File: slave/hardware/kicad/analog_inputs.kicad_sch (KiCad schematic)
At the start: 105 parts, among them IC10 TSV772IST, IC11 TSV772IST, IC12 TSV772IST, IC8 TSV772IST, IC9 TSV772IST

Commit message: feat(HW): start control sheet implementation
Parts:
- renumbered C38 to C20, C45 to C21, C44 to C22, C51 to C23, C40 to C24, C47 to C25, C39 to C26, C46 to C27, C52 to C28, C53 to C29, C54 to C30, C55 to C31, C41 to C32, C48 to C33, C42 to C34, C49 to C35, C56 to C36, C57 to C37, C43 to C38, C50 to C39, D24 to D10, D13 to D11, D20 to D12, D12 to D13, D19 to D14, D25 to D15, D26 to D16, D27 to D17, D28 to D18, D14 to D19, D21 to D20, D15 to D21, D29 to D23, D30 to D24, D16 to D25, D23 to D26, D11 to D7, D18 to D8, D17 to D9, IC8 to IC5, IC11 to IC6, IC9 to IC7, IC12 to IC8, IC10 to IC9, R20 to R10, R33 to R11, R22 to R12, R35 to R13, R24 to R14, R37 to R15, R30 to R16, R43 to R17, R44 to R18, R45 to R19, R46 to R20, R47 to R21, R48 to R22, R49 to R23, R19 to R24, R32 to R25, R21 to R26, R34 to R27, R23 to R28, R36 to R29, R25 to R30, R38 to R31, R50 to R32, R51 to R33, R52 to R34, R53 to R35, R54 to R36, R55 to R37, R56 to R38, R57 to R39, R26 to R40, R39 to R41, R27 to R42, R40 to R43, R28 to R44, R41 to R45, R29 to R46, R42 to R47, R18 to R8, R31 to R9, TP23 to TP10, TP10 to TP11, TP11 to TP12, TP14 to TP13, TP15 to TP14, TP24 to TP15, TP25 to TP16, TP26 to TP17, TP27 to TP18, TP16 to TP19, TP17 to TP20, TP18 to TP21, TP19 to TP22, TP28 to TP23, TP29 to TP24, TP20 to TP25, TP21 to TP26, TP13 to TP7, TP12 to TP8, TP22 to TP9

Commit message: feat(HW): add digital input circuit files
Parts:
- renumbered C20 to C40, C21 to C41, C22 to C42, C23 to C43, C24 to C44, C25 to C45, C26 to C46, C27 to C47, C28 to C48, C29 to C49, C30 to C50, C31 to C51, C32 to C52, C33 to C53, C34 to C54, C35 to C55, C36 to C56, C37 to C57, C38 to C58, C39 to C59, D7 to D27, D8 to D28, D9 to D29, D10 to D30, D11 to D31, D12 to D32, D13 to D33, D14 to D34, D15 to D35, D16 to D36, D17 to D37, D18 to D38, D19 to D39, D20 to D40, D21 to D41, D22 to D42, D23 to D43, D24 to D44, D25 to D45, D26 to D46, IC5 to IC10, IC6 to IC11, IC7 to IC12, IC8 to IC13, IC9 to IC14, R8 to R48, R9 to R49, R10 to R50, R11 to R51, R12 to R52, R13 to R53, R14 to R54, R15 to R55, R16 to R56, R17 to R57, R18 to R58, R19 to R59, R20 to R60, R21 to R61, R22 to R62, R23 to R63, R24 to R64, R25 to R65, R26 to R66, R27 to R67, R28 to R68, R29 to R69, R30 to R70, R31 to R71, R32 to R72, R33 to R73, R34 to R74, R35 to R75, R36 to R76, R37 to R77, R38 to R78, R39 to R79, R40 to R80, R41 to R81, R42 to R82, R43 to R83, R44 to R84, R45 to R85, R46 to R86, R47 to R87, TP7 to TP27, TP8 to TP28, TP9 to TP29, TP10 to TP30, TP11 to TP31, TP12 to TP32, TP13 to TP33, TP14 to TP34, TP15 to TP35, TP16 to TP36, TP17 to TP37, TP18 to TP38, TP19 to TP39, TP20 to TP40, TP21 to TP41, TP22 to TP42, TP23 to TP43, TP24 to TP44, TP25 to TP45, TP26 to TP46

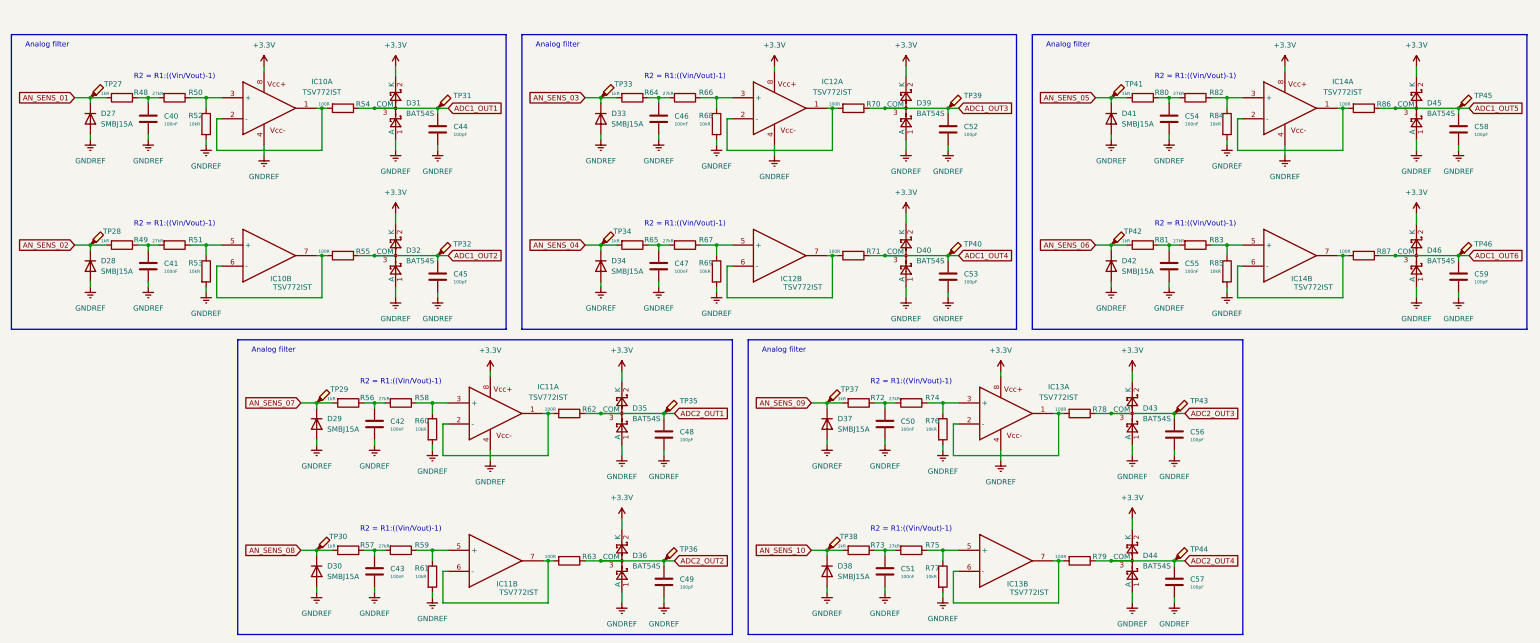
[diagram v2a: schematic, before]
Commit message: refactor(HW): reduce analog inputs and update MCU analog connections
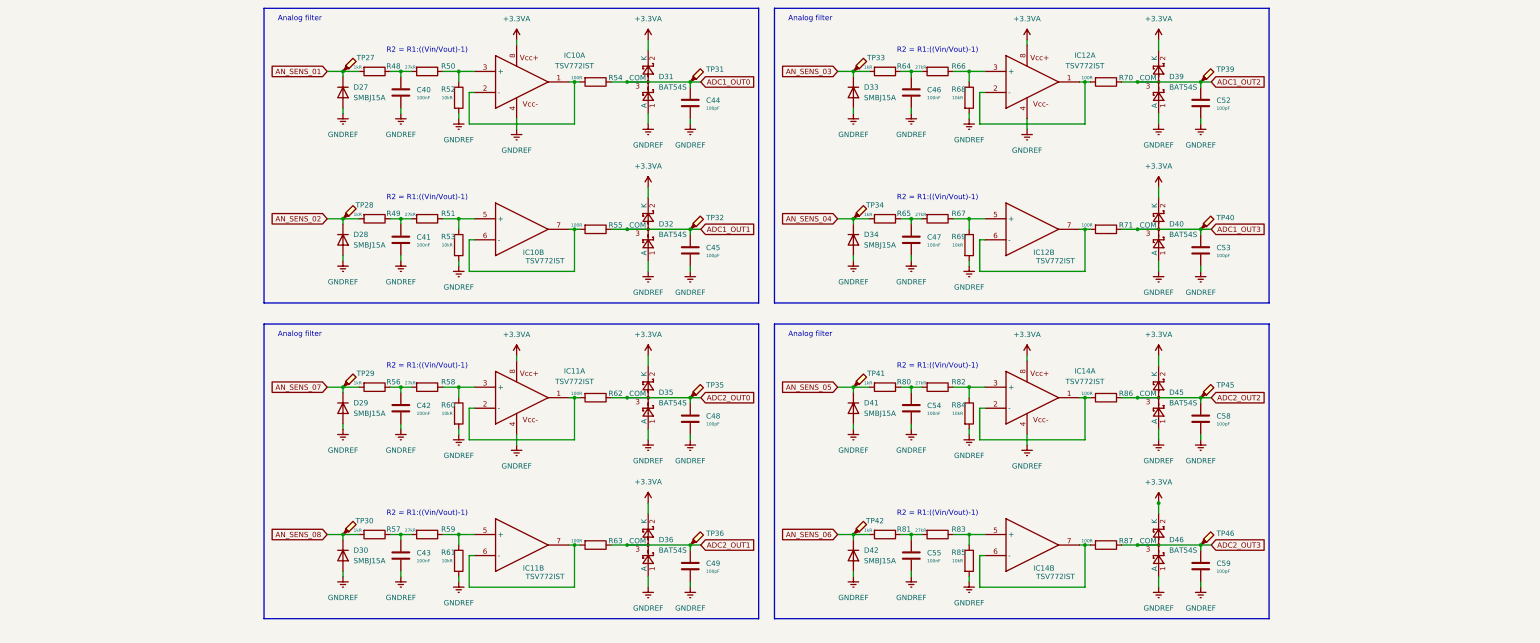
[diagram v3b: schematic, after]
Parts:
- removed C50, C51: 100nF, Capacitor_SMD:C_0201_0603Metric, symbol Device:C
- removed C56, C57: 100pF, Capacitor_SMD:C_0201_0603Metric, symbol Device:C
- removed D37, D38: SMBJ15A, Diode_SMD:D_SMB, symbol Device:D
- removed D43, D44: BAT54S, Package_TO_SOT_SMD:SOT-23, symbol Diode:BAT54S
- removed IC13: TSV772IST, SOP65P490X110-8N, symbol Datalogger Slave:TSV772IST
- removed R72, R73: 1kR, Resistor_SMD:R_0805_2012Metric, symbol Device:R
- removed R74, R75: 27kR, Resistor_SMD:R_0805_2012Metric, symbol Device:R
- removed R76, R77: 10kR, Resistor_SMD:R_0805_2012Metric, symbol Device:R
- removed R78, R79: 100R, Resistor_SMD:R_0805_2012Metric, symbol Device:R
- removed TP37, TP38, TP43, TP44: (no value), TestPoint:TestPoint_Pad_2.0x2.0mm, symbol Connector:TestPoint_Probe
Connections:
- net ADC1_OUT4 is gone; now on net ADC1_OUT3: C53.1, D40.3 (COM), R71.1, TP40.1
- net ADC1_OUT5 is gone; now on net ADC2_OUT2: C58.1, D45.3 (COM), R86.1, TP45.1
- net ADC1_OUT6 is gone; now on net ADC2_OUT3: C59.1, D46.3 (COM), R87.1, TP46.1
- net ADC1_OUT1: now also C45.1, D32.3 (COM), R55.1, TP32.1; no longer C44.1, D31.3 (COM), R54.1, TP31.1
- net ADC1_OUT2: now also C52.1, D39.3 (COM), R70.1, TP39.1; no longer C45.1, D32.3 (COM), R55.1, TP32.1
- net ADC1_OUT3: no longer C52.1, D39.3 (COM), R70.1, TP39.1
- net ADC2_OUT1: now also C49.1, D36.3 (COM), R63.1, TP36.1; no longer C48.1, D35.3 (COM), R62.1, TP35.1
- net ADC2_OUT2: no longer C49.1, D36.3 (COM), R63.1, TP36.1
- net +3.3V renamed +3.3VA
- new net ADC1_OUT0: C44.1, D31.3 (COM), R54.1, TP31.1
- new net ADC2_OUT0: C48.1, D35.3 (COM), R62.1, TP35.1
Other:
- moved on the sheet: C40, C41, C42, C43, C44, C45, C46, C47, C48, C49, C52, C53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

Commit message: feat(HW): create communication schematic with CAN and I2C level shifter
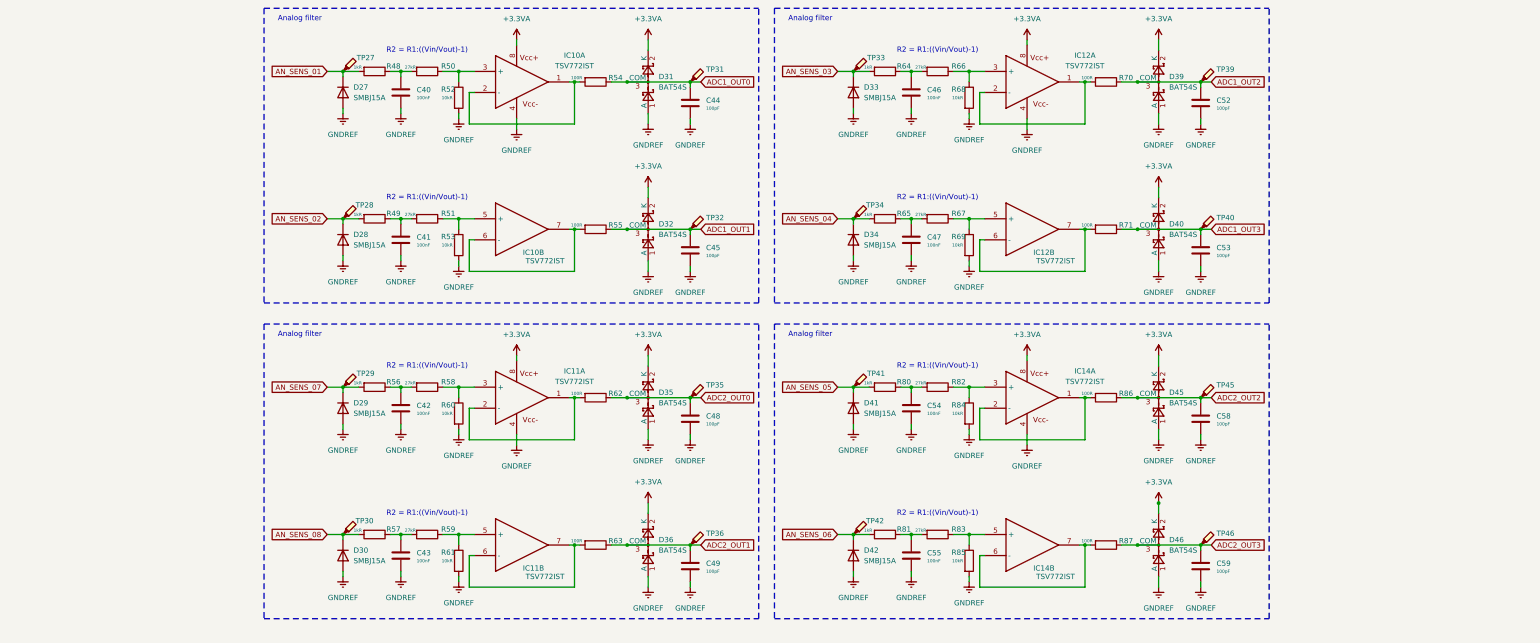
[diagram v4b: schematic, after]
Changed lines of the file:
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@@
 		(stroke
 			(width 0)
-			(type default)
+			(type dash_dot)
 		)
 	)
@@
 		(stroke
 			(width 0)
-			(type default)
+			(type dash_dot)
 		)
 	)
@@
 		(stroke
 			(width 0)
-			(type default)
+			(type dash_dot)
 		)
 	)
@@
 		(stroke
 			(width 0)
-			(type default)
+			(type dash_dot)
 		)
 	)
@@
 		(stroke
 			(width 0)
-			(type default)
+			(type dash_dot)
 		)
 	)
@@
 		(stroke
 			(width 0)
-			(type default)
+			(type dash_dot)
 		)
 	)
@@
 		(stroke
 			(width 0)
-			(type default)
+			(type dash_dot)
 		)
 	)
@@
 		(stroke
 			(width 0)
-			(type default)
+			(type dash_dot)
 		)
 	)
@@
 		(stroke
 			(width 0)
-			(type default)
+			(type dash_dot)
 		)
 	)
@@
 		(stroke
 			(width 0)
-			(type default)
+			(type dash_dot)
 		)
 	)
@@
 		(stroke
 			(width 0)
-			(type default)
+			(type dash_dot)
 		)
 	)
@@
 		(stroke
 			(width 0)
-			(type default)
+			(type dash_dot)
 		)
 	)
@@
 		(stroke
 			(width 0)
-			(type default)
+			(type dash_dot)
 		)
 	)
@@
 		(stroke
 			(width 0)
-			(type default)
+			(type dash_dot)
 		)
 	)
@@
 		(stroke
 			(width 0)
-			(type default)
+			(type dash_dot)
 		)
 	)
@@
 		(stroke
 			(width 0)
-			(type default)
-		)
-	)
+			(type dash_dot)
+		)
+	)

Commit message: refactor(HW): rename components and fix reference designators
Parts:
- renumbered C40 to C20, C41 to C21, C42 to C22, C43 to C23, C44 to C24, C45 to C25, C48 to C26, C49 to C27, C46 to C28, C47 to C29, C54 to C30, C55 to C31, C52 to C32, C53 to C33, C58 to C34, C59 to C35, D30 to D10, D31 to D11, D32 to D12, D35 to D13, D36 to D14, D33 to D15, D34 to D16, D41 to D17, D42 to D18, D39 to D19, D40 to D20, D45 to D21, D46 to D22, D27 to D7, D28 to D8, D29 to D9, IC10 to IC5, IC11 to IC6, IC12 to IC7, IC14 to IC8, R56 to R10, R57 to R11, R50 to R12, R51 to R13, R58 to R14, R59 to R15, R52 to R16, R53 to R17, R60 to R18, R61 to R19, R54 to R20, R55 to R21, R62 to R22, R63 to R23, R64 to R24, R65 to R25, R80 to R26, R81 to R27, R66 to R28, R67 to R29, R82 to R30, R83 to R31, R68 to R32, R69 to R33, R84 to R34, R85 to R35, R70 to R36, R71 to R37, R86 to R38, R87 to R39, R48 to R8, R49 to R9, TP30 to TP10, TP31 to TP11, TP32 to TP12, TP35 to TP13, TP36 to TP14, TP33 to TP15, TP34 to TP16, TP41 to TP17, TP42 to TP18, TP39 to TP19, TP40 to TP20, TP45 to TP21, TP46 to TP22, TP27 to TP7, TP28 to TP8, TP29 to TP9
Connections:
- net AN_SENS_05: now also D9.1 (K), R10.2, TP9.1; no longer D17.1 (K), R26.2, TP17.1
- net AN_SENS_06: now also D10.1 (K), R11.2, TP10.1; no longer D18.1 (K), R27.2, TP18.1
- net AN_SENS_07: now also D17.1 (K), R26.2, TP17.1; no longer D9.1 (K), R10.2, TP9.1
- net AN_SENS_08: now also D18.1 (K), R27.2, TP18.1; no longer D10.1 (K), R11.2, TP10.1

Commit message: feat(HW): add footprints and configure component properties
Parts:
- IC5, IC6, IC7, IC8: footprint SOP65P490X110-8N -> Datalogger:SOP65P490X110-8N
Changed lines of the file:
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@@
 			)
 		)
-		(property "Footprint" "SOP65P490X110-8N"
+		(property "Footprint" "Datalogger:SOP65P490X110-8N"
 			(at 284.48 190.17 0)
 			(hide yes)
@@
 			)
 		)
-		(property "Footprint" "SOP65P490X110-8N"
+		(property "Footprint" "Datalogger:SOP65P490X110-8N"
 			(at 161.29 225.73 0)
 			(hide yes)
@@
 			)
 		)
-		(property "Footprint" "SOP65P490X110-8N"
+		(property "Footprint" "Datalogger:SOP65P490X110-8N"
 			(at 161.29 266.37 0)
 			(hide yes)
@@
 			)
 		)
-		(property "Footprint" "SOP65P490X110-8N"
+		(property "Footprint" "Datalogger:SOP65P490X110-8N"
 			(at 284.48 225.73 0)
 			(hide yes)
@@
 			)
 		)
-		(property "Footprint" "SOP65P490X110-8N"
+		(property "Footprint" "Datalogger:SOP65P490X110-8N"
 			(at 161.29 301.93 0)
 			(hide yes)
@@
 			)
 		)
-		(property "Footprint" "SOP65P490X110-8N"
+		(property "Footprint" "Datalogger:SOP65P490X110-8N"
 			(at 284.48 266.37 0)
 			(hide yes)
@@
 			)
 		)
-		(property "Footprint" "SOP65P490X110-8N"
+		(property "Footprint" "Datalogger:SOP65P490X110-8N"
 			(at 284.48 301.93 0)
 			(hide yes)
@@
 			)
 		)
-		(property "Footprint" "SOP65P490X110-8N"
+		(property "Footprint" "Datalogger:SOP65P490X110-8N"
 			(at 161.29 190.17 0)
 			(hide yes)

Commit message: fix(HW): resolve KiCad ERC warnings
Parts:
- removed IC5, IC6, IC7, IC8: TSV772IST, Datalogger:SOP65P490X110-8N, symbol Datalogger Slave:TSV772IST
- added IC5, IC6, IC7, IC9: TSV772IST, Datalogger:SOP65P490X110-8N, symbol Datalogger:TSV772IST
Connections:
- net +3.3VA: now also IC5.8, IC6.8, IC7.8, IC9.8
- net GNDREF: now also IC5.4, IC6.4, IC7.4, IC9.4
- net at R23.2: now also IC7.6 (-), IC7.7
- net at R36.2: now also IC5.1, IC5.2 (-)
- net at R28.1, R32.1: now also IC5.3 (+)
- net at R30.1, R34.1: now also IC6.3 (+)
- net at R29.1, R33.1: now also IC5.5 (+)
- net at R13.1, R17.1: now also IC9.5 (+)
- net at R21.2: now also IC9.6 (-), IC9.7
- net at R31.1, R35.1: now also IC6.5 (+)
- net at R12.1, R16.1: now also IC9.3 (+)
- net at R37.2: now also IC5.6 (-), IC5.7
- net at R22.2: now also IC7.1, IC7.2 (-)
- net at R14.1, R18.1: now also IC7.3 (+)
- net at R15.1, R19.1: now also IC7.5 (+)
- net at R20.2: now also IC9.1, IC9.2 (-)
- net at R38.2: now also IC6.1, IC6.2 (-)
- net at R39.2: now also IC6.6 (-), IC6.7

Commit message: feat(HW): begin PCB layout design
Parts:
- C20, C21, C22, C23, C24, C25, C26, C27, C28, C29, C30, C31, C32, C33, C34, C35: footprint Capacitor_SMD:C_0201_0603Metric -> Capacitor_SMD:C_0603_1608Metric
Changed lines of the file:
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@@
 			)
 		)
-		(property "Footprint" "Capacitor_SMD:C_0201_0603Metric"
+		(property "Footprint" "Capacitor_SMD:C_0603_1608Metric"
 			(at 314.6552 180.34 0)
 			(hide yes)
@@
 			)
 		)
-		(property "Footprint" "Capacitor_SMD:C_0201_0603Metric"
+		(property "Footprint" "Capacitor_SMD:C_0603_1608Metric"
 			(at 314.6552 139.7 0)
 			(hide yes)
@@
 			)
 		)
-		(property "Footprint" "Capacitor_SMD:C_0201_0603Metric"
+		(property "Footprint" "Capacitor_SMD:C_0603_1608Metric"
 			(at 244.8052 213.36 0)
 			(hide yes)
@@
 			)
 		)
-		(property "Footprint" "Capacitor_SMD:C_0201_0603Metric"
+		(property "Footprint" "Capacitor_SMD:C_0603_1608Metric"
 			(at 191.4652 215.9 0)
 			(hide yes)
@@
 			)
 		)
-		(property "Footprint" "Capacitor_SMD:C_0201_0603Metric"
+		(property "Footprint" "Capacitor_SMD:C_0603_1608Metric"
 			(at 191.4652 180.34 0)
 			(hide yes)
@@
 			)
 		)
-		(property "Footprint" "Capacitor_SMD:C_0201_0603Metric"
+		(property "Footprint" "Capacitor_SMD:C_0603_1608Metric"
 			(at 191.4652 139.7 0)
 			(hide yes)
@@
 			)
 		)
-		(property "Footprint" "Capacitor_SMD:C_0201_0603Metric"
+		(property "Footprint" "Capacitor_SMD:C_0603_1608Metric"
 			(at 121.6152 101.6 0)
 			(hide yes)
@@
 			)
 		)
-		(property "Footprint" "Capacitor_SMD:C_0201_0603Metric"
+		(property "Footprint" "Capacitor_SMD:C_0603_1608Metric"
 			(at 314.6552 215.9 0)
 			(hide yes)
@@
 			)
 		)
-		(property "Footprint" "Capacitor_SMD:C_0201_0603Metric"
+		(property "Footprint" "Capacitor_SMD:C_0603_1608Metric"
 			(at 121.6152 177.8 0)
 			(hide yes)
@@
 			)
 		)
-		(property "Footprint" "Capacitor_SMD:C_0201_0603Metric"
+		(property "Footprint" "Capacitor_SMD:C_0603_1608Metric"
 			(at 244.8052 177.8 0)
 			(hide yes)
@@
 			)
 		)
-		(property "Footprint" "Capacitor_SMD:C_0201_0603Metric"
+		(property "Footprint" "Capacitor_SMD:C_0603_1608Metric"
 			(at 314.6552 104.14 0)
 			(hide yes)
@@
 			)
 		)
-		(property "Footprint" "Capacitor_SMD:C_0201_0603Metric"
+		(property "Footprint" "Capacitor_SMD:C_0603_1608Metric"
 			(at 244.8052 137.16 0)
 			(hide yes)
@@
 			)
 		)
-		(property "Footprint" "Capacitor_SMD:C_0201_0603Metric"
+		(property "Footprint" "Capacitor_SMD:C_0603_1608Metric"
 			(at 121.6152 137.16 0)
 			(hide yes)
@@
 			)
 		)
-		(property "Footprint" "Capacitor_SMD:C_0201_0603Metric"
+		(property "Footprint" "Capacitor_SMD:C_0603_1608Metric"
 			(at 244.8052 101.6 0)
 			(hide yes)
@@
 			)
 		)
-		(property "Footprint" "Capacitor_SMD:C_0201_0603Metric"
+		(property "Footprint" "Capacitor_SMD:C_0603_1608Metric"
 			(at 121.6152 213.36 0)
 			(hide yes)
@@
 			)
 		)
-		(property "Footprint" "Capacitor_SMD:C_0201_0603Metric"
+		(property "Footprint" "Capacitor_SMD:C_0603_1608Metric"
 			(at 191.4652 104.14 0)
 			(hide yes)
